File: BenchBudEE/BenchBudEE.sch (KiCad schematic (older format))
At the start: 0 parts

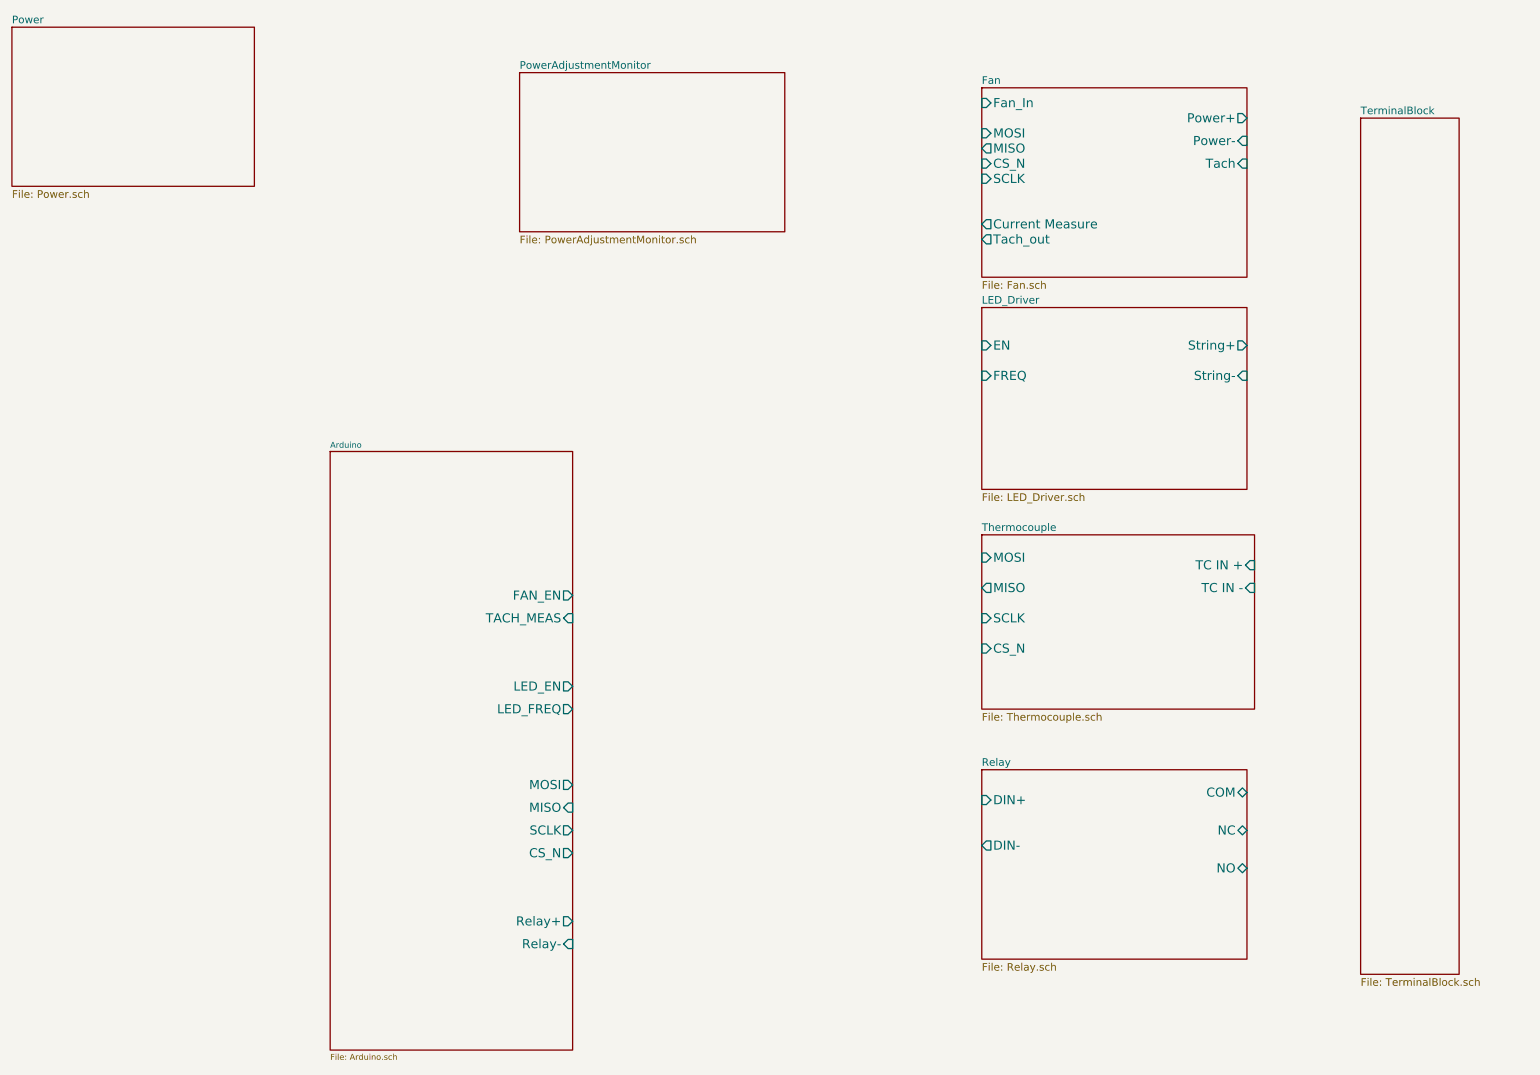
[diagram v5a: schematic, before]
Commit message: Power Control Conditioning and monitoring block diagram
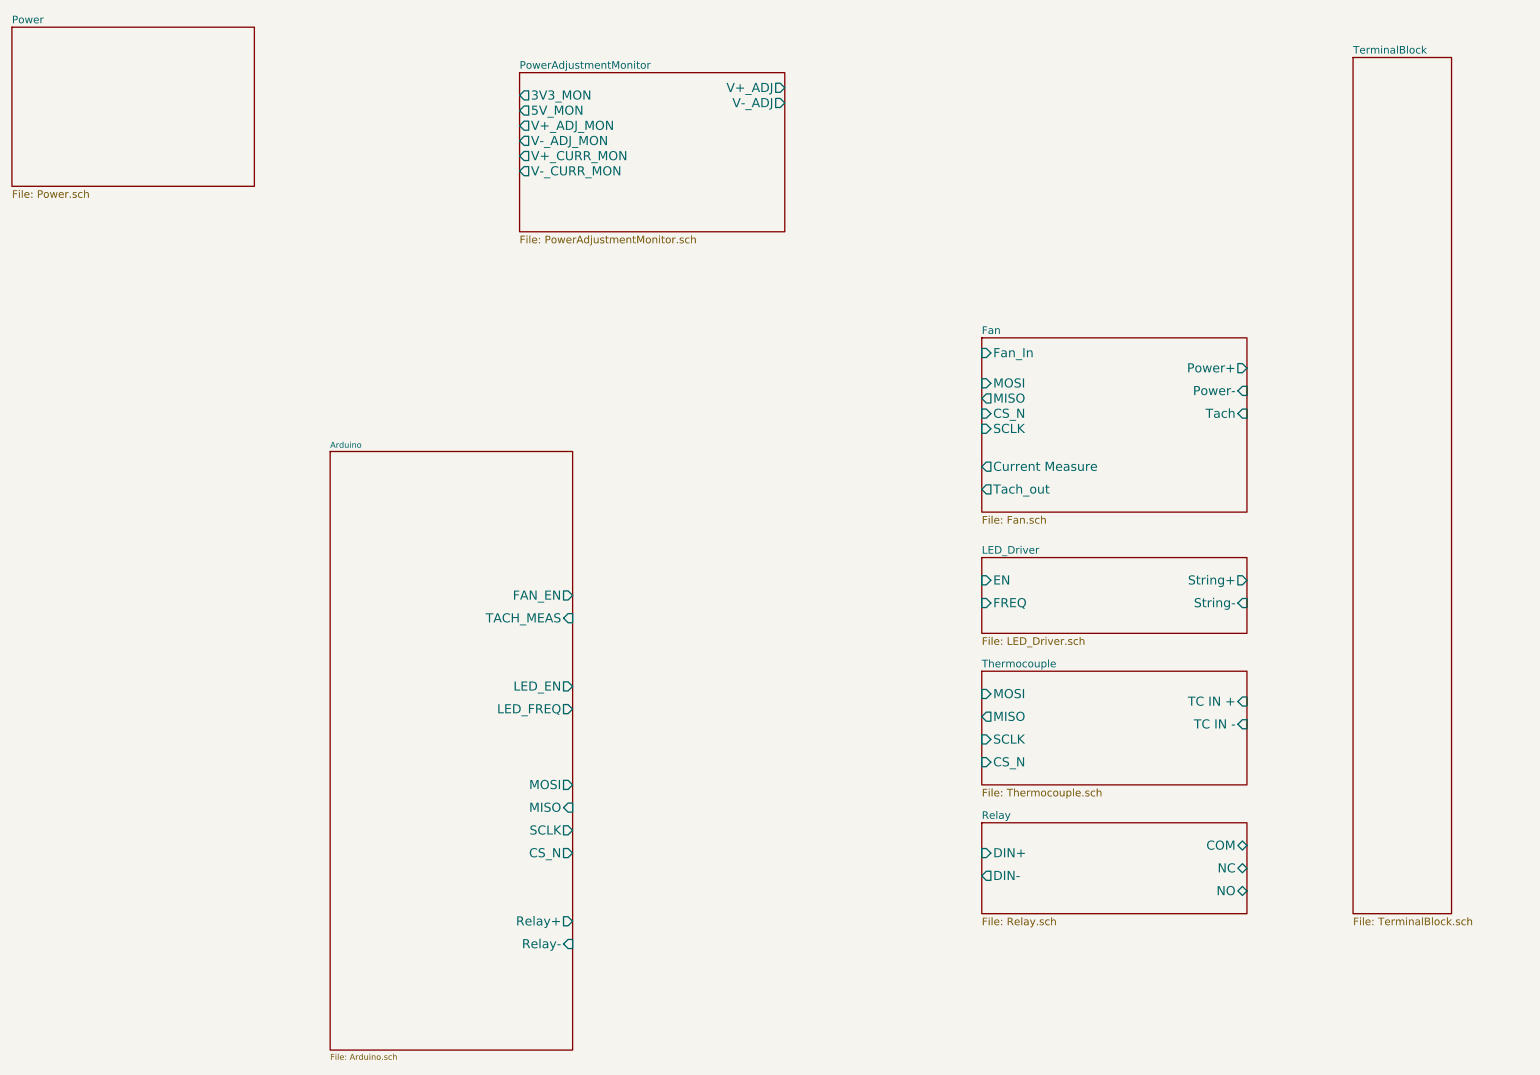
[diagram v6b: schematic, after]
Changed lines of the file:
@@
 Sheet 1 9
 Title ""
-Date "8 feb 2014"
+Date "9 feb 2014"
 Rev ""
 Comp ""
@@
 $EndSheet
 $Sheet
-S 7100 4050 1800 1150
+S 7100 4950 1750 750
 U 52ED1C3D
 F0 "Thermocouple" 50
 F1 "Thermocouple.sch" 50
-F2 "TC IN +" I R 8900 4250 60
-F3 "TC IN -" I R 8900 4400 60
-F4 "MOSI" I L 7100 4200 60
-F5 "MISO" O L 7100 4400 60
-F6 "SCLK" I L 7100 4600 60
-F7 "CS_N" I L 7100 4800 60
+F2 "TC IN +" I R 8850 5150 60
+F3 "TC IN -" I R 8850 5300 60
+F4 "MOSI" I L 7100 5100 60
+F5 "MISO" O L 7100 5250 60
+F6 "SCLK" I L 7100 5400 60
+F7 "CS_N" I L 7100 5550 60
 $EndSheet
 $Sheet
-S 7100 2550 1750 1200
+S 7100 4200 1750 500
 U 52ED1C90
 F0 "LED_Driver" 50
 F1 "LED_Driver.sch" 50
-F2 "EN" I L 7100 2800 60
-F3 "FREQ" I L 7100 3000 60
-F4 "String+" O R 8850 2800 60
-F5 "String-" I R 8850 3000 60
+F2 "EN" I L 7100 4350 60
+F3 "FREQ" I L 7100 4500 60
+F4 "String+" O R 8850 4350 60
+F5 "String-" I R 8850 4500 60
 $EndSheet
 $Sheet
-S 7100 1100 1750 1250
+S 7100 2750 1750 1150
 U 52ED1CA7
 F0 "Fan" 50
 F1 "Fan.sch" 50
-F2 "Power+" O R 8850 1300 60
-F3 "Power-" I R 8850 1450 60
-F4 "Tach" I R 8850 1600 60
-F5 "Tach_out" O L 7100 2100 60
-F6 "Fan_In" I L 7100 1200 60
-F7 "Current Measure" O L 7100 2000 60
-F8 "MOSI" I L 7100 1400 60
-F9 "MISO" O L 7100 1500 60
-F10 "CS_N" I L 7100 1600 60
-F11 "SCLK" I L 7100 1700 60
+F2 "Power+" O R 8850 2950 60
+F3 "Power-" I R 8850 3100 60
+F4 "Tach" I R 8850 3250 60
+F5 "Tach_out" O L 7100 3750 60
+F6 "Fan_In" I L 7100 2850 60
+F7 "Current Measure" O L 7100 3600 60
+F8 "MOSI" I L 7100 3050 60
+F9 "MISO" O L 7100 3150 60
+F10 "CS_N" I L 7100 3250 60
+F11 "SCLK" I L 7100 3350 60
 $EndSheet
 $Sheet
-S 9600 1300 650  5650
+S 9550 900  650  5650
 U 52ED1CD3
 F0 "TerminalBlock" 50
 F1 "TerminalBlock.sch" 50
-$EndSheet
-$Sheet
-S 7100 5600 1750 1250
-U 52ED1C4D
-F0 "Relay" 50
-F1 "Relay.sch" 50
-F2 "DIN+" I L 7100 5800 60
-F3 "DIN-" O L 7100 6100 60
-F4 "NC" B R 8850 6000 60
-F5 "NO" B R 8850 6250 60
-F6 "COM" B R 8850 5750 60
 $EndSheet
 $Sheet
@@
 F0 "PowerAdjustmentMonitor" 50
 F1 "PowerAdjustmentMonitor.sch" 50
+F2 "V+_ADJ" O R 5800 1100 60
+F3 "V-_ADJ" O R 5800 1200 60
+F4 "3V3_MON" O L 4050 1150 60
+F5 "5V_MON" O L 4050 1250 60
+F6 "V+_ADJ_MON" O L 4050 1350 60
+F7 "V-_ADJ_MON" O L 4050 1450 60
+F8 "V+_CURR_MON" O L 4050 1550 60
+F9 "V-_CURR_MON" O L 4050 1650 60
 $EndSheet
 $Sheet
@@
 F1 "Power.sch" 50
 $EndSheet
+$Sheet
+S 7100 5950 1750 600
+U 52ED1C4D
+F0 "Relay" 50
+F1 "Relay.sch" 50
+F2 "DIN+" I L 7100 6150 60
+F3 "DIN-" O L 7100 6300 60
+F4 "NC" B R 8850 6250 60
+F5 "NO" B R 8850 6400 60
+F6 "COM" B R 8850 6100 60
+$EndSheet
 $EndSCHEMATC

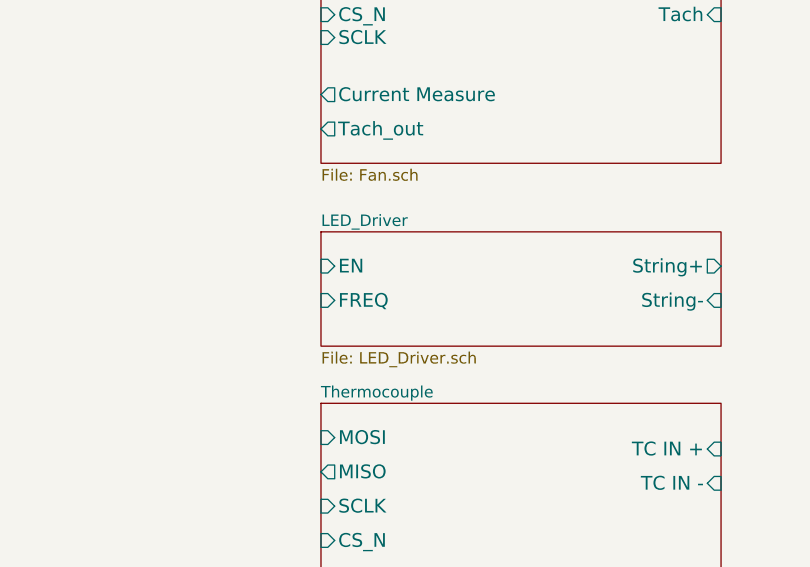
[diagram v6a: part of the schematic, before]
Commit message: LED Driver block diagram
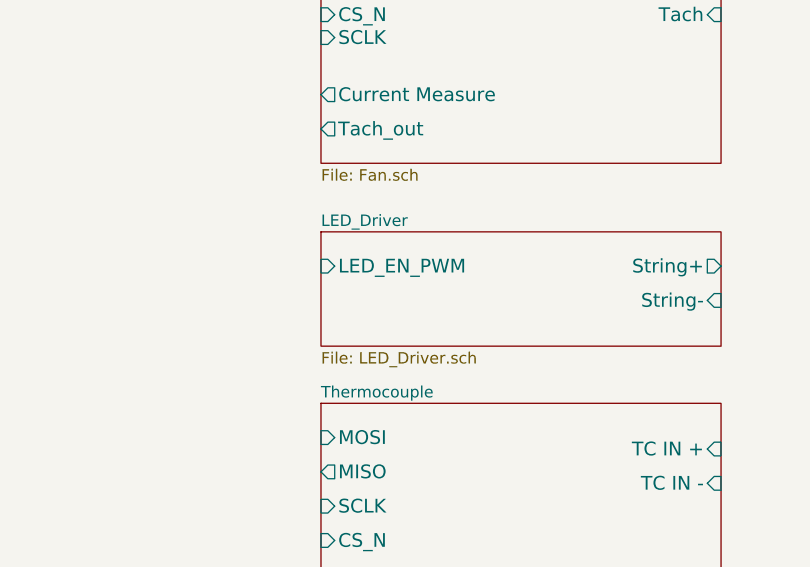
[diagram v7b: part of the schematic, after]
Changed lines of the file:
@@
 F0 "LED_Driver" 50
 F1 "LED_Driver.sch" 50
-F2 "EN" I L 7100 4350 60
-F3 "FREQ" I L 7100 4500 60
-F4 "String+" O R 8850 4350 60
-F5 "String-" I R 8850 4500 60
+F2 "String+" O R 8850 4350 60
+F3 "String-" I R 8850 4500 60
+F4 "LED_EN_PWM" I L 7100 4350 60
 $EndSheet
 $Sheet
